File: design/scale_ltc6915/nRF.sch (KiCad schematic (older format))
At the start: 30 parts, among them J1 USB_B_Micro, J2 Conn_02x03_Odd_Even, Q1 IRLML6401, SW1 SW_SPST, SW2 ON/OFF switch, U1 MDBT42Q, U2 BQ21040, U3 TPS7A0233PDBV, Y1 Q13FC1350000400

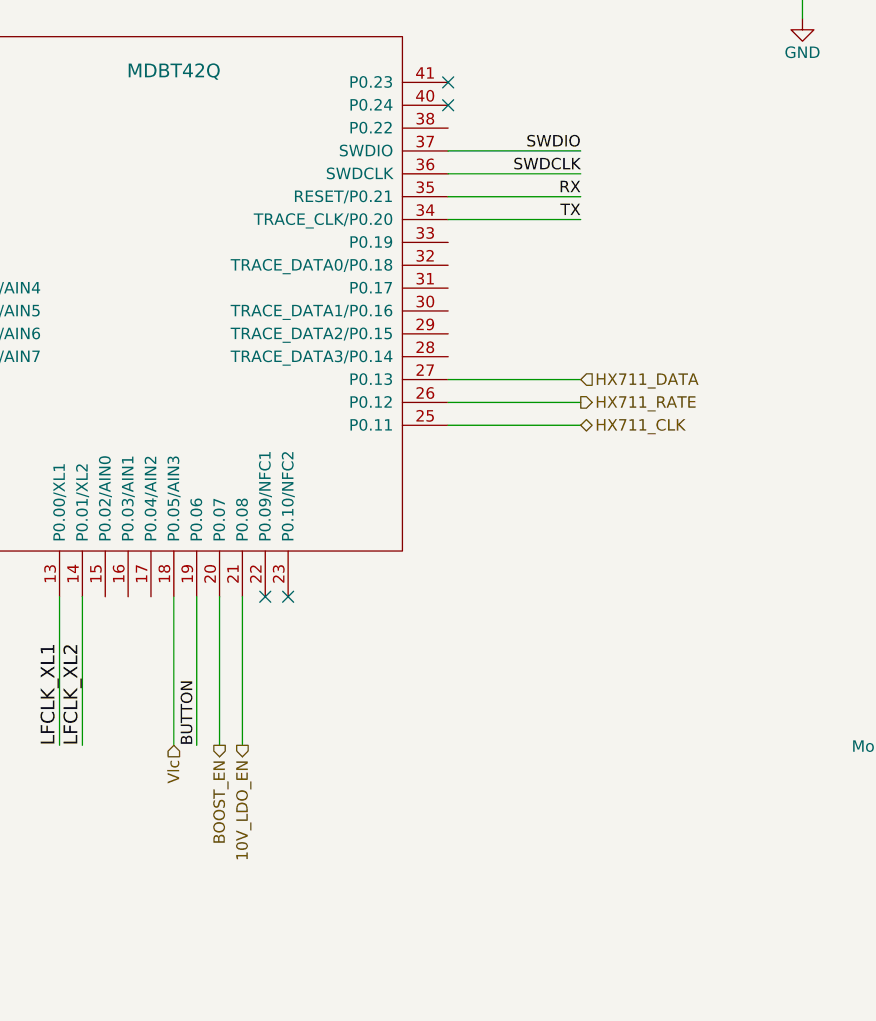
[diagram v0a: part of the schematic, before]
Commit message: Schematics, BoM updated. New project added - scale_ltc6915
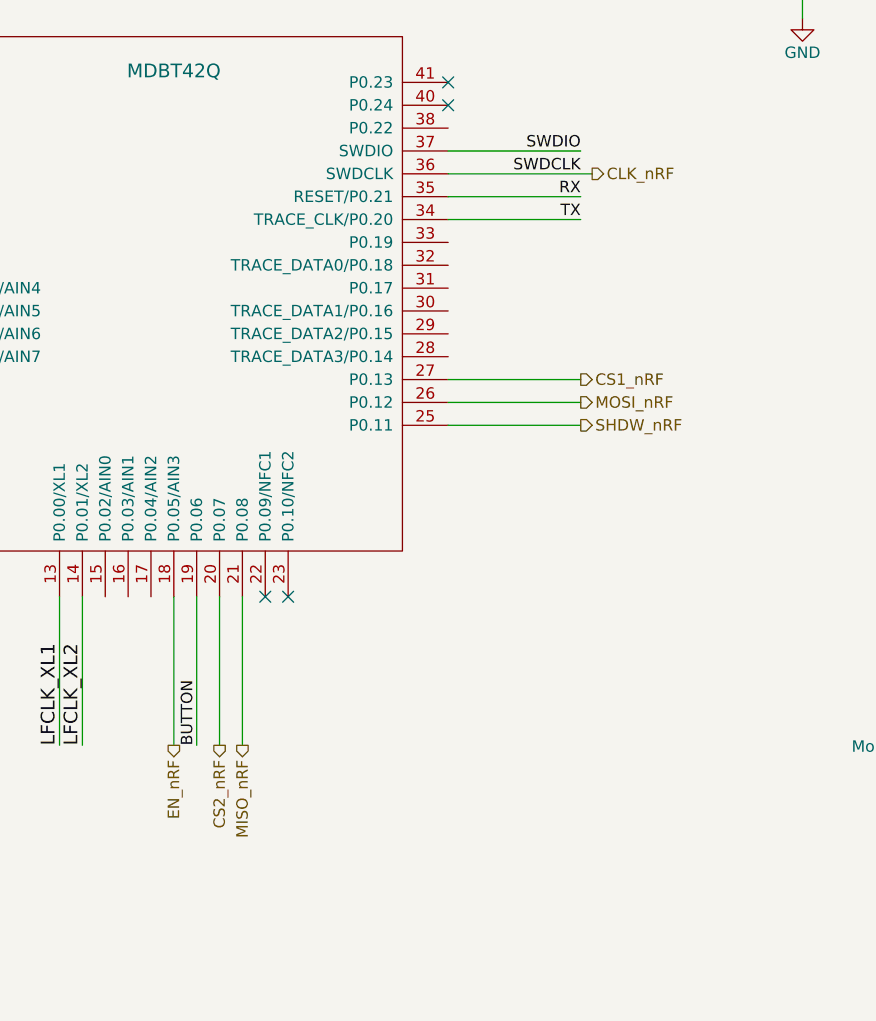
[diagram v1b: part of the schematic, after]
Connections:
- net 10V_LDO_EN renamed MISO_nRF
- net BOOST_EN renamed CS2_nRF
- net HX711_CLK renamed SHDW_nRF
- net HX711_DATA renamed CS1_nRF
- net HX711_RATE renamed MOSI_nRF
- net SWDCLK renamed CLK_nRF
- net Vlc renamed EN_nRF
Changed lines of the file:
@@
 	7800 3700 7220 3700
-Wire Wire Line
-	7220 3800 7800 3800
 Wire Wire Line
 	7800 3900 7220 3900
@@
 Text HLabel 7550 1350 2    50   Output ~ 0
 VBAT
-Text HLabel 7800 4700 2    50   Input ~ 0
-HX711_DATA
-Text HLabel 7800 4800 2    50   Output ~ 0
-HX711_RATE
-Text HLabel 7800 4900 2    50   BiDi ~ 0
-HX711_CLK
 Text Label 6120 6300 1    50   ~ 0
 BUTTON
-Text HLabel 6220 6300 3    50   Output ~ 0
-BOOST_EN
-Text HLabel 6320 6300 3    50   Output ~ 0
-10V_LDO_EN
-Text HLabel 6020 6300 3    50   Input ~ 0
-Vlc
 Wire Wire Line
 	6020 6300 6020 5650
@@
 Wire Wire Line
 	7800 4700 7220 4700
+Text HLabel 7800 4900 2    50   Output ~ 0
+SHDW_nRF
+Text HLabel 7800 4700 2    50   Output ~ 0
+CS1_nRF
+Text HLabel 7800 4800 2    50   Output ~ 0
+MOSI_nRF
+Text HLabel 7850 3800 2    50   Output ~ 0
+CLK_nRF
+Text HLabel 6220 6300 3    50   Output ~ 0
+CS2_nRF
+Text HLabel 6320 6300 3    50   Output ~ 0
+MISO_nRF
+Text HLabel 6020 6300 3    50   Output ~ 0
+EN_nRF
+Wire Wire Line
+	7220 3800 7850 3800
 $EndSCHEMATC

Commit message: updated schematic of scale_ltc6915, fixed issues
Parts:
- added J4: Conn_01x04, Connector_PinHeader_2.00mm:PinHeader_1x04_P2.00mm_Vertical, symbol Connector_Generic:Conn_01x04
- U3: symbol scale_hx711-rescue:TLV70013_SOT23-5-Regulator_Linear -> scale_ltc6915.pro-rescue:TLV70013_SOT23-5-Regulator_Linear
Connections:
- net CLK_nRF: now also U1.25 (P0.11); no longer J2.3 (Pin_3), U1.36 (SWDCLK)
- net CS1_nRF: now also U1.26 (P0.12); no longer U1.27 (P0.13)
- net CS2_nRF: now also U1.29 (TRACE_DATA2/P0.15); no longer U1.20 (P0.07)
- net EN_nRF: now also U1.21 (P0.08); no longer U1.18 (P0.05/AIN3)
- net GND: now also J2.4 (Pin_4); no longer J2.6 (Pin_6)
- net MISO_nRF: now also U1.28 (TRACE_DATA3/P0.14); no longer U1.21 (P0.08)
- net MOSI_nRF: now also U1.20 (P0.07); no longer U1.26 (P0.12)
- net RX: now also J2.5 (Pin_5); no longer J2.2 (Pin_2)
- net SHDW_nRF: now also U1.27 (P0.13); no longer U1.25 (P0.11)
- net TX: now also J2.6 (Pin_6); no longer J2.5 (Pin_5)
- net VDD: now also J2.2 (Pin_2); no longer J2.4 (Pin_4)
- net 10V_LDO_EN: now reaches U1.16 (P0.03/AIN1)
- net BOOST_EN: now reaches U1.17 (P0.04/AIN2)
- net EINK_BUSY: now reaches U1.2 (P0.25)
- net EINK_RST: now reaches U1.3 (P0.26)
- net GPIO3: now reaches U1.30 (TRACE_DATA1/P0.16)
- net GPIO3: now also J4.4 (Pin_4)
- net GPIO2: now reaches U1.31 (P0.17)
- net GPIO2: now also J4.3 (Pin_3)
- net GPIO1: now reaches U1.32 (TRACE_DATA0/P0.18)
- net GPIO1: now also J4.2 (Pin_2)
- net GPIO0: now reaches U1.33 (P0.19)
- net GPIO0: now also J4.1 (Pin_1)
- net EINK_CS: now reaches U1.4 (P0.27)
- net EINK_SCLK: now reaches U1.5 (P0.28/AIN4)
- net EINK_SDIO: now reaches U1.6 (P0.29/AIN5)
- new net SWDCLK: J2.3 (Pin_3), U1.36 (SWDCLK)
- new net Vlc: U1.18 (P0.05/AIN3)
- no-connect marks 9 -> 13
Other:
- moved on the sheet: J2
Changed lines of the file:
@@
 Text Label 2550 4580 3    60   ~ 0
 LFCLK_XL2
-Text Label 1350 6975 0    50   ~ 0
+Text Label 1450 6975 0    50   ~ 0
 SWDIO
-Text Label 1350 7075 0    50   ~ 0
+Text Label 1450 7075 0    50   ~ 0
 SWDCLK
-Text Label 2550 6975 2    50   ~ 0
+Text Label 1450 7175 0    50   ~ 0
 RX
-Text Label 1350 7175 0    50   ~ 0
+Text Label 2650 7175 2    50   ~ 0
 TX
 $Comp
 L sense:VDD #PWR05
 U 1 1 5E71D407
-P 2700 7025
-F 0 "#PWR05" H 2700 6875 50  0001 C CNN
-F 1 "VDD" H 2700 7175 50  0000 C CNN
-F 2 "" H 2700 7025 60  0000 C CNN
-F 3 "" H 2700 7025 60  0000 C CNN
-	1    2700 7025
+P 2801 6900
+F 0 "#PWR05" H 2801 6750 50  0001 C CNN
+F 1 "VDD" H 2801 7050 50  0000 C CNN
+F 2 "" H 2801 6900 60  0000 C CNN
+F 3 "" H 2801 6900 60  0000 C CNN
+	1    2801 6900
 	1    0    0    -1
 $EndComp
@@
 Text Notes 1180 3310 0    60   ~ 0
 To use the Internal DC/DC\nregulator we need external\ninductors
-Text Notes 1600 6675 0    60   ~ 0
+Text Notes 1600 6700 0    60   ~ 0
 For programming \nand debugging \nthe nRF controller
 Text Notes 1900 4830 0    60   ~ 0
@@
 L sense:GND #PWR04
 U 1 1 5E71D403
-P 2700 7225
-F 0 "#PWR04" H 2700 6975 50  0001 C CNN
-F 1 "GND" H 2700 7075 50  0000 C CNN
-F 2 "" H 2700 7225 60  0000 C CNN
-F 3 "" H 2700 7225 60  0000 C CNN
-	1    2700 7225
+P 2800 7250
+F 0 "#PWR04" H 2800 7000 50  0001 C CNN
+F 1 "GND" H 2800 7100 50  0000 C CNN
+F 2 "" H 2800 7250 60  0000 C CNN
+F 3 "" H 2800 7250 60  0000 C CNN
+	1    2800 7250
 	1    0    0    -1
 $EndComp
@@
 L sense:Conn_02x03_Odd_Even J2
 U 1 1 5D8500C4
-P 1900 7075
-F 0 "J2" H 1950 7392 50  0000 C CNN
-F 1 "Conn_02x03_Odd_Even" H 1950 7301 50  0000 C CNN
-F 2 "Connector_PinHeader_2.00mm:PinHeader_2x03_P2.00mm_Vertical" H 1900 7075 50  0001 C CNN
-F 3 "~" H 1900 7075 50  0001 C CNN
-	1    1900 7075
-	1    0    0    -1
-$EndComp
-Wire Wire Line
-	2700 7225 2700 7175
-Wire Wire Line
-	2700 7175 2200 7175
-Wire Wire Line
-	2200 7075 2700 7075
-Wire Wire Line
-	2700 7075 2700 7025
-Wire Wire Line
-	2200 6975 2550 6975
-Wire Wire Line
-	1350 6975 1700 6975
-Wire Wire Line
-	1700 7075 1350 7075
-Wire Wire Line
-	1350 7175 1700 7175
+P 2000 7075
+F 0 "J2" H 2050 7392 50  0000 C CNN
+F 1 "Conn_02x03_Odd_Even" H 2050 7301 50  0000 C CNN
+F 2 "Connector_PinHeader_2.00mm:PinHeader_2x03_P2.00mm_Vertical" H 2000 7075 50  0001 C CNN
+F 3 "~" H 2000 7075 50  0001 C CNN
+	1    2000 7075
+	1    0    0    -1
+$EndComp
+Wire Wire Line
+	2300 7175 2650 7175
+Wire Wire Line
+	1450 6975 1800 6975
+Wire Wire Line
+	1800 7075 1450 7075
+Wire Wire Line
+	1450 7175 1800 7175
 $Comp
 L sense:SW_SPST SW1
@@
 NoConn ~ 7220 3400
 NoConn ~ 7220 3500
-$Comp
-L sense:MDBT42Q U1
-U 1 1 5E71D3F5
-P 6020 4100
-F 0 "U1" H 5105 2700 60  0000 C CNN
-F 1 "MDBT42Q" H 6020 4850 60  0000 C CNN
-F 2 "sense_fp:mdbt42Q" H 5820 5200 60  0001 C CNN
-F 3 "" H 5820 5200 60  0000 C CNN
-	1    6020 4100
-	1    0    0    -1
-$EndComp
 Wire Wire Line
 	5520 5650 5520 6300
@@
 	4820 4800 4200 4800
 Wire Wire Line
-	4820 4700 4200 4700
-Wire Wire Line
 	3965 3450 4820 3450
 Wire Wire Line
@@
 Wire Wire Line
 	7800 3700 7220 3700
+Wire Wire Line
+	7220 3800 7800 3800
 Wire Wire Line
 	7800 3900 7220 3900
@@
 VBAT
 $Comp
-L scale_hx711-rescue:TLV70013_SOT23-5-Regulator_Linear U?
+L scale_ltc6915.pro-rescue:TLV70013_SOT23-5-Regulator_Linear U?
 U 1 1 5E60E4CD
 P 9300 1450
@@
 NoConn ~ 6520 5650
 Wire Wire Line
-	6220 6300 6220 5650
+	7800 4900 7220 4900
+Wire Wire Line
+	7220 4800 7800 4800
+Wire Wire Line
+	7800 4700 7220 4700
+Text HLabel 4240 4400 0    50   Output ~ 0
+EINK_SDIO
+Text HLabel 4230 4300 0    50   Output ~ 0
+EINK_SCLK
+Text HLabel 4240 4200 0    50   Output ~ 0
+EINK_CS
+Text HLabel 4240 4100 0    50   Output ~ 0
+EINK_RST
+Text HLabel 4240 4000 0    50   Input ~ 0
+EINK_BUSY
+Wire Wire Line
+	4240 4000 4820 4000
+Wire Wire Line
+	4820 4200 4240 4200
+Wire Wire Line
+	4820 4400 4240 4400
+Wire Wire Line
+	2801 6900 2801 6975
+Wire Wire Line
+	2801 6975 2300 6975
+Wire Wire Line
+	2800 7250 2800 7075
+Wire Wire Line
+	2800 7075 2300 7075
+NoConn ~ 4820 4600
+NoConn ~ 4820 4500
+Wire Wire Line
+	4820 4100 4240 4100
+Wire Wire Line
+	4230 4300 4820 4300
+$Comp
+L sense:MDBT42Q U1
+U 1 1 5E71D3F5
+P 6020 4100
+F 0 "U1" H 5105 2700 60  0000 C CNN
+F 1 "MDBT42Q" H 6020 4850 60  0000 C CNN
+F 2 "sense_fp:mdbt42Q" H 5820 5200 60  0001 C CNN
+F 3 "" H 5820 5200 60  0000 C CNN
+	1    6020 4100
+	1    0    0    -1
+$EndComp
+Wire Wire Line
+	4820 4700 4200 4700
+NoConn ~ 5720 5650
+Wire Wire Line
+	6220 5650 6220 6300
 Wire Wire Line
 	6320 5650 6320 6300
-Wire Wire Line
-	7800 4900 7220 4900
-Wire Wire Line
-	7220 4800 7800 4800
-Wire Wire Line
-	7800 4700 7220 4700
+NoConn ~ 7220 3600
+$Comp
+L Connector_Generic:Conn_01x04 J4
+U 1 1 5E6691E5
+P 10400 4450
+F 0 "J4" H 10480 4442 50  0000 L CNN
+F 1 "Conn_01x04" H 10480 4351 50  0000 L CNN
+F 2 "Connector_PinHeader_2.00mm:PinHeader_1x04_P2.00mm_Vertical" H 10400 4450 50  0001 C CNN
+F 3 "~" H 10400 4450 50  0001 C CNN
+	1    10400 4450
+	1    0    0    -1
+$EndComp
+Text Label 9900 4350 0    50   ~ 0
+GPIO0
+Text Label 9900 4450 0    50   ~ 0
+GPIO1
+Text Label 9900 4550 0    50   ~ 0
+GPIO2
+Text Label 9900 4650 0    50   ~ 0
+GPIO3
+Wire Wire Line
+	9900 4650 10200 4650
+Wire Wire Line
+	10200 4550 9900 4550
+Wire Wire Line
+	9900 4450 10200 4450
+Wire Wire Line
+	10200 4350 9900 4350
+Text Label 7800 4100 2    50   ~ 0
+GPIO0
+Text Label 7800 4200 2    50   ~ 0
+GPIO1
+Text Label 7800 4300 2    50   ~ 0
+GPIO2
+Text Label 7800 4400 2    50   ~ 0
+GPIO3
+Wire Wire Line
+	7220 4400 7800 4400
+Wire Wire Line
+	7800 4100 7220 4100
+Wire Wire Line
+	7220 4200 7800 4200
+Wire Wire Line
+	7800 4300 7220 4300
+Text HLabel 5920 6300 3    50   Output ~ 0
+BOOST_EN
+Text HLabel 5820 6300 3    50   Output ~ 0
+10V_LDO_EN
+Text HLabel 6020 6300 3    50   Input ~ 0
+Vlc
+Text HLabel 7800 4700 2    50   Output ~ 0
+SHDW_nRF
+Text HLabel 7800 4800 2    50   Output ~ 0
+CS1_nRF
+Text HLabel 6220 6300 3    50   Output ~ 0
+MOSI_nRF
 Text HLabel 7800 4900 2    50   Output ~ 0
-SHDW_nRF
-Text HLabel 7800 4700 2    50   Output ~ 0
-CS1_nRF
-Text HLabel 7800 4800 2    50   Output ~ 0
-MOSI_nRF
-Text HLabel 7850 3800 2    50   Output ~ 0
 CLK_nRF
-Text HLabel 6220 6300 3    50   Output ~ 0
+Text HLabel 7800 4500 2    50   Output ~ 0
 CS2_nRF
+Text HLabel 7800 4600 2    50   Output ~ 0
+MISO_nRF
 Text HLabel 6320 6300 3    50   Output ~ 0
-MISO_nRF
-Text HLabel 6020 6300 3    50   Output ~ 0
 EN_nRF
 Wire Wire Line
-	7220 3800 7850 3800
+	5820 6300 5820 5650
+Wire Wire Line
+	5920 5650 5920 6300
+Wire Wire Line
+	7800 4500 7220 4500
+Wire Wire Line
+	7220 4600 7800 4600
 $EndSCHEMATC
